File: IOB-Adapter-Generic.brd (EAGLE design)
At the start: 17.8 x 38.1 mm, 5 parts

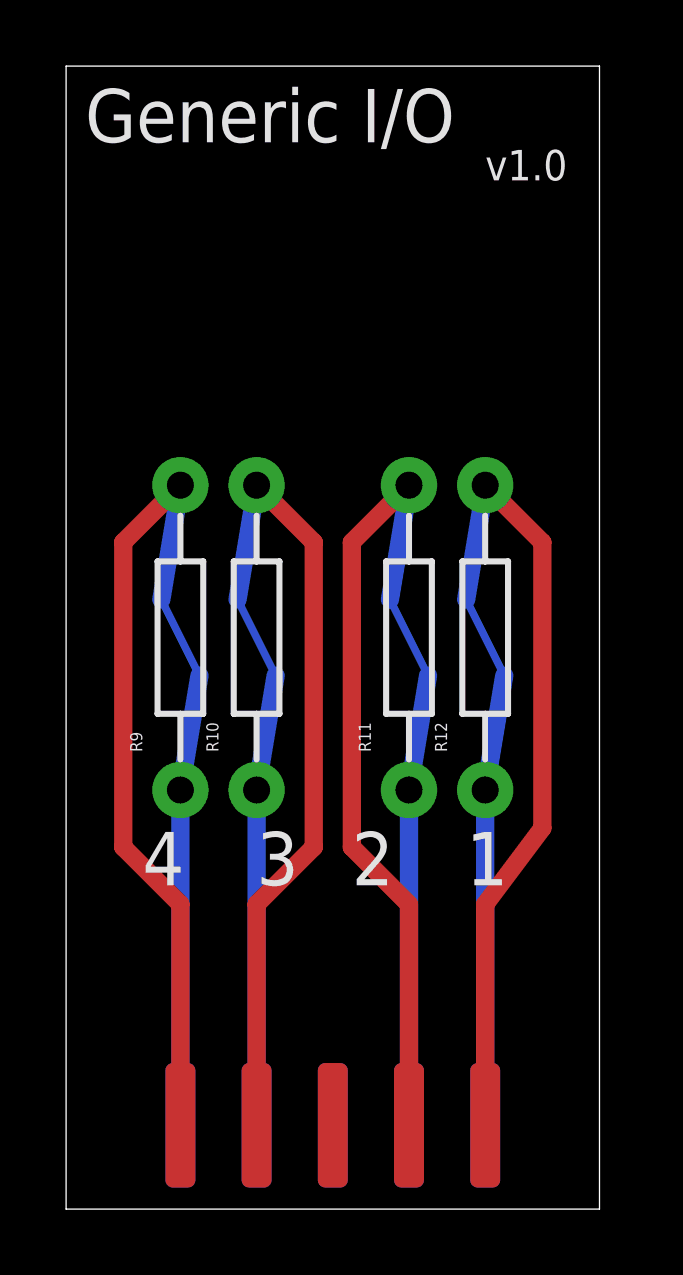
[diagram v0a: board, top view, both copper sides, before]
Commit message: change from edge to PTH mount
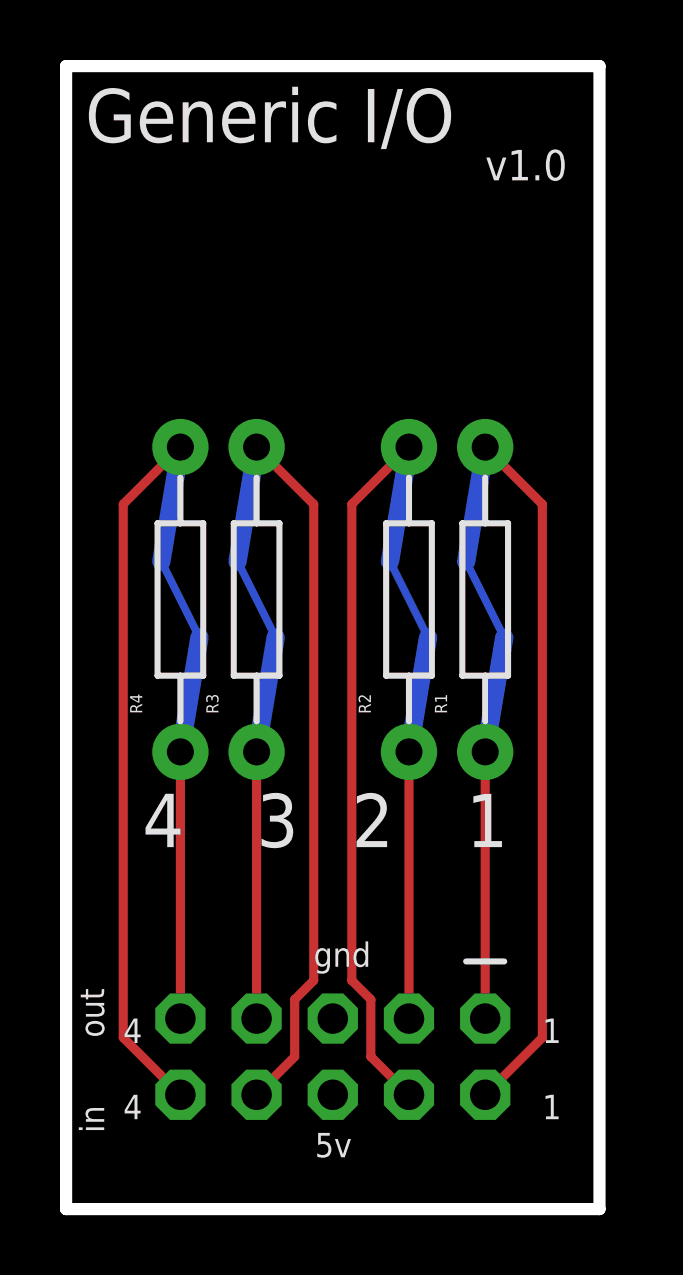
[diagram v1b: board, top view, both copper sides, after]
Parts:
- removed R10, R11, R12, R9: NOSTUFF, SPCoast:CUT-R
- added R1, R2, R3, R4: NOSTUFF, SPCoast:CUT-R
- JP1: value CONNECTOR-M05X2EDGE -> CONNECTOR-M05X2; device SPCoast:2X5-EDGE -> SPCoast:IOB-V3-MODULE
- moved JP1 5.08 mm to (8.89, 5.08), flipped to the bottom, turned to 270 degrees
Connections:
- net N$1: now also R1.P2; no longer R9.P2
- net N$2: now also R2.P2; no longer R10.P2
- net N$3: now also R3.P2; no longer R11.P2
- net N$4: now also R4.P2; no longer R12.P2
- net P1: now also R1.P1; no longer R9.P1
- net P2: now also R2.P1; no longer R10.P1
- net P3: now also R3.P1; no longer R11.P1
- net P4: now also R4.P1; no longer R12.P1
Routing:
- net N$4: track 11.2 -> 8.89 mm
- net N$3: track 11.2 -> 8.89 mm
- net N$2: track 11.2 -> 8.89 mm
- net N$1: track 11.2 -> 8.89 mm
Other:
- board text added: "GENERIC I/O"
- board text added: "JP1"
- board text added: "R1"
- board text added: "R2"
- board text added: "R3"
- board text added: "R4"
- board text removed: "I/O Driver Board"
- board text removed: "R10"
- board text removed: "R11"
- board text removed: "R12"
- board text removed: "R9"
